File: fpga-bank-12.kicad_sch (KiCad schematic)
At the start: 1 part, among them U4 XC7K160T-FFG676

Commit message: [#65754] Rename project
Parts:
- added U34: XCAU25P-2FFVB676I, antmicro-footprints:BGA-676_27x27mm_Layout26x26_P1x1mm_FFVB676, symbol antmicroFPGAChips:XCAU25P-2FFVB676I
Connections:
- net +3V3: now also U34.AC15 (VCCO_84), U34.E14 (VCCO_87), U34.E9 (VCCO_86), U34.H10 (VCCO_86), U34.H15 (VCCO_87), U34.Y14 (VCCO_84)
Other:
- title: SO-DIMM DDR5 Tester -> RDIMM DDR5 Tester

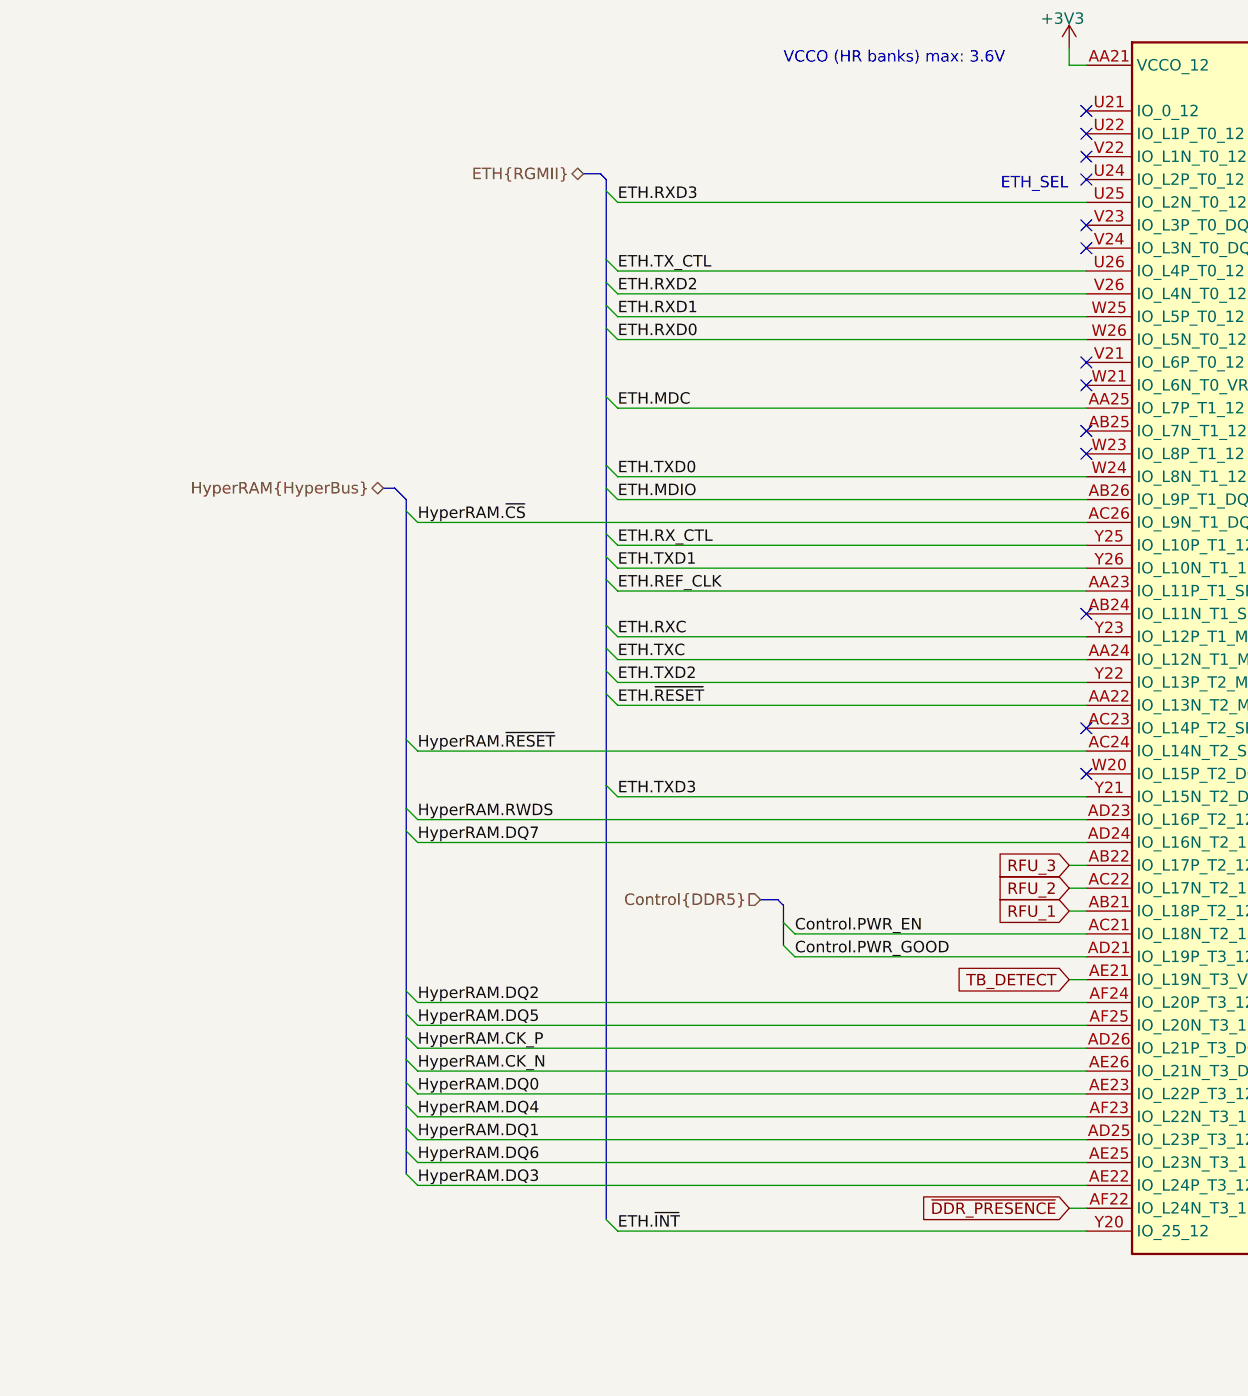
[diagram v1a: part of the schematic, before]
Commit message: [#66727] Reconnect HyperRam and ETH RGMII to HP bank 67
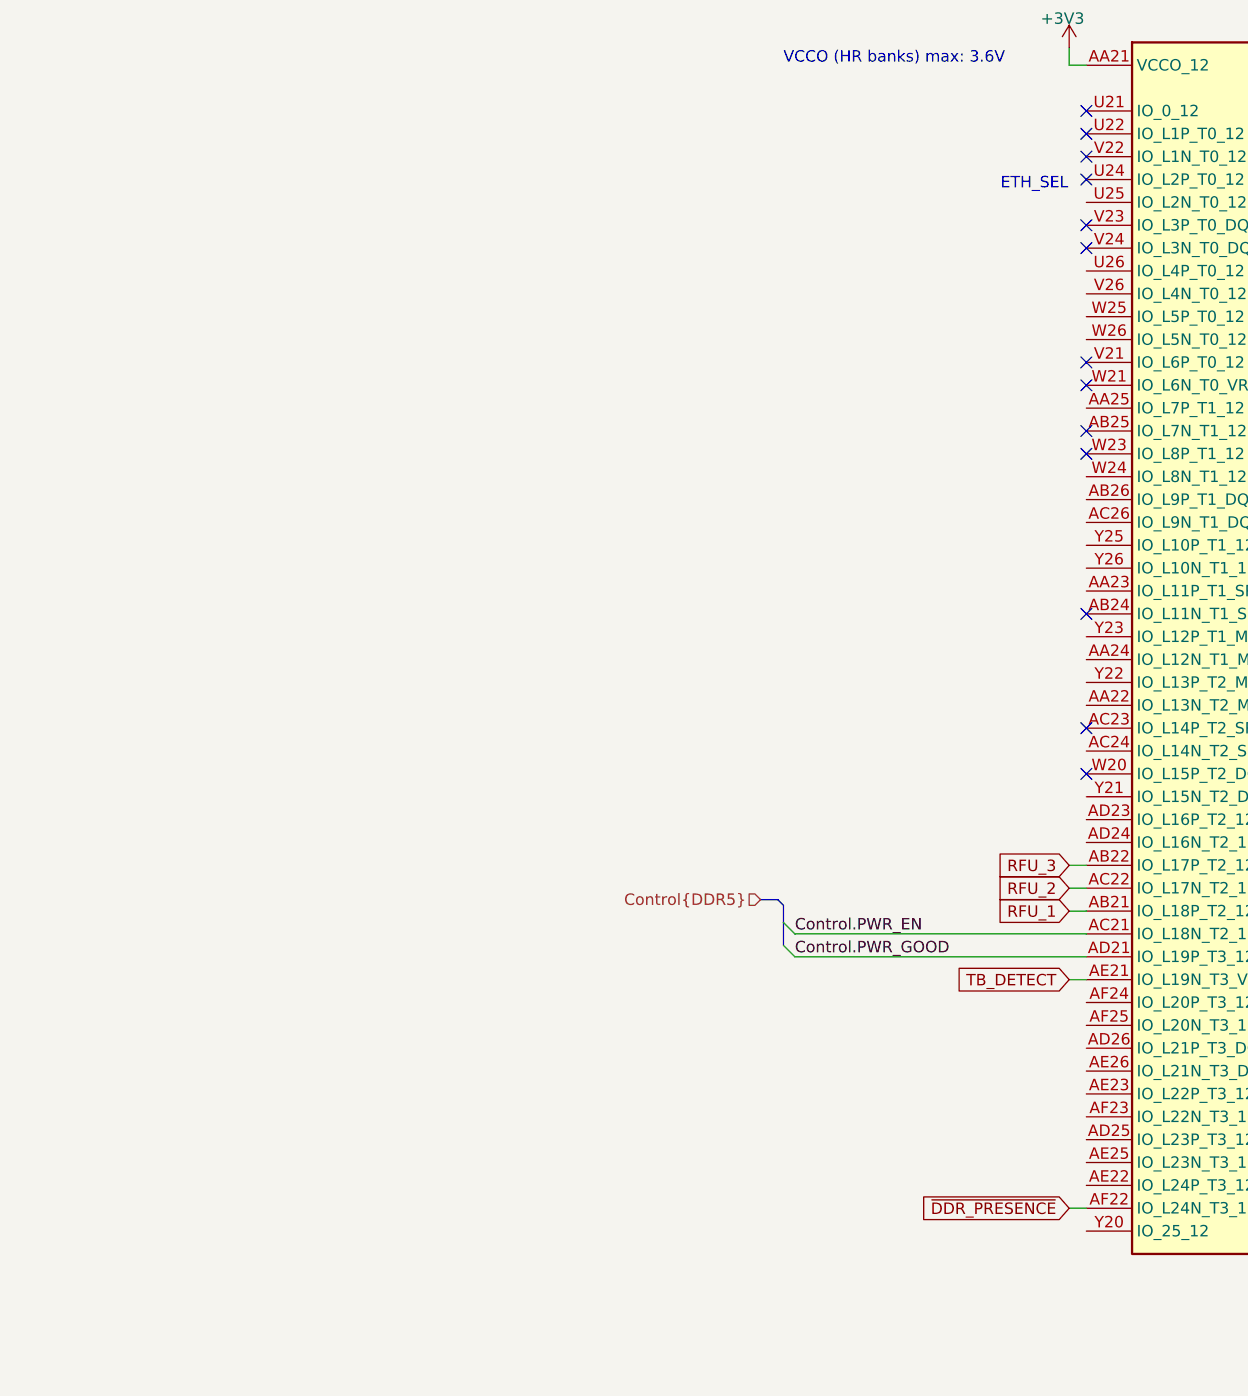
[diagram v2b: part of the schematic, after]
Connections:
- net ETH.MDC: no longer names the net of U4.AA25 (IO_L7P_T1_12)
- net ETH.MDIO: no longer names the net of U4.AB26 (IO_L9P_T1_DQS_12)
- net ETH.REF_CLK: no longer names the net of U4.AA23 (IO_L11P_T1_SRCC_12)
- net ETH.RXC: no longer names the net of U4.Y23 (IO_L12P_T1_MRCC_12)
- net ETH.RXD0: no longer names the net of U4.W26 (IO_L5N_T0_12)
- net ETH.RXD1: no longer names the net of U4.W25 (IO_L5P_T0_12)
- net ETH.RXD2: no longer names the net of U4.V26 (IO_L4N_T0_12)
- net ETH.RXD3: no longer names the net of U4.U25 (IO_L2N_T0_12)
- net ETH.RX_CTL: no longer names the net of U4.Y25 (IO_L10P_T1_12)
- net ETH.TXC: no longer names the net of U4.AA24 (IO_L12N_T1_MRCC_12)
- net ETH.TXD0: no longer names the net of U4.W24 (IO_L8N_T1_12)
- net ETH.TXD1: no longer names the net of U4.Y26 (IO_L10N_T1_12)
- net ETH.TXD2: no longer names the net of U4.Y22 (IO_L13P_T2_MRCC_12)
- net ETH.TXD3: no longer names the net of U4.Y21 (IO_L15N_T2_DQS_12)
- net ETH.TX_CTL: no longer names the net of U4.U26 (IO_L4P_T0_12)
- net ETH.~{INT}: no longer names the net of U4.Y20 (IO_25_12)
- net ETH.~{RESET}: no longer names the net of U4.AA22 (IO_L13N_T2_MRCC_12)
- net HyperRAM.CK_N: no longer names the net of U4.AE26 (IO_L21N_T3_DQS_12)
- net HyperRAM.CK_P: no longer names the net of U4.AD26 (IO_L21P_T3_DQS_12)
- net HyperRAM.DQ0: no longer names the net of U4.AE23 (IO_L22P_T3_12)
- net HyperRAM.DQ1: no longer names the net of U4.AD25 (IO_L23P_T3_12)
- net HyperRAM.DQ2: no longer names the net of U4.AF24 (IO_L20P_T3_12)
- net HyperRAM.DQ3: no longer names the net of U4.AE22 (IO_L24P_T3_12)
- net HyperRAM.DQ4: no longer names the net of U4.AF23 (IO_L22N_T3_12)
- net HyperRAM.DQ5: no longer names the net of U4.AF25 (IO_L20N_T3_12)
- net HyperRAM.DQ6: no longer names the net of U4.AE25 (IO_L23N_T3_12)
- net HyperRAM.DQ7: no longer names the net of U4.AD24 (IO_L16N_T2_12)
- net HyperRAM.RWDS: no longer names the net of U4.AD23 (IO_L16P_T2_12)
- net HyperRAM.~{CS}: no longer names the net of U4.AC26 (IO_L9N_T1_DQS_12)
- net HyperRAM.~{RESET}: no longer names the net of U4.AC24 (IO_L14N_T2_SRCC_12)
